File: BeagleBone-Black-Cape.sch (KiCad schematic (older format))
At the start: 2 parts

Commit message: FOUR LAYER BOARD CHANGE. We still need to adapt the other subsystems for four layers
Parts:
- gave numbers to parts that had none: 2
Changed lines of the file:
@@
 	3800 2900 3700 2900
 $Comp
-L BeagleBone-Black-Cape-rescue:Conn_02x23_Odd_Even-Connector_Generic P?
+L BeagleBone-Black-Cape-rescue:Conn_02x23_Odd_Even-Connector_Generic P101
 U 1 1 55DF7DBA
 P 4000 3600
-F 0 "P?" H 4000 4800 50  0000 C CNN
+F 0 "P101" H 4000 4800 50  0000 C CNN
 F 1 "BeagleBone_Black_Header" V 4050 3650 50  0000 C CNN
 F 2 "Socket_BeagleBone_Black:Socket_BeagleBone_Black" H 4000 2750 60  0001 C CNN
@@
 $EndComp
 $Comp
-L BeagleBone-Black-Cape-rescue:Conn_02x23_Odd_Even-Connector_Generic P?
+L BeagleBone-Black-Cape-rescue:Conn_02x23_Odd_Even-Connector_Generic P102
 U 1 1 55DF7DE1
 P 6200 3600
-F 0 "P?" H 6200 4800 50  0000 C CNN
+F 0 "P102" H 6200 4800 50  0000 C CNN
 F 1 "BeagleBone_Black_Header" V 6250 3650 50  0000 C CNN
 F 2 "Socket_BeagleBone_Black:Socket_BeagleBone_Black" H 6200 2750 60  0001 C CNN
@@
 $EndComp
 $Comp
-L power:GND #PWR0101
+L power:GND #PWR0107
 U 1 1 614B6213
 P 3000 2500
-F 0 "#PWR0101" H 3000 2250 50  0001 C CNN
+F 0 "#PWR0107" H 3000 2250 50  0001 C CNN
 F 1 "GND" H 3005 2327 50  0000 C CNN
 F 2 "" H 3000 2500 50  0001 C CNN

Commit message: Recovered the .lib for flash symbol. Relinked in schematic
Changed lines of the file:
@@
 	3650 4900 4050 4900
 $Comp
-L power:GND #PWR0105
+L BeagleBone-Black-Cape-rescue:GND-power #PWR0105
 U 1 1 614B4DBF
 P 4050 4900
@@
 	4050 4900 4450 4900
 $Comp
-L power:GND #PWR0109
+L BeagleBone-Black-Cape-rescue:GND-power #PWR0109
 U 1 1 614B5823
 P 5100 2500
@@
 $EndComp
 $Comp
-L power:GND #PWR0101
+L BeagleBone-Black-Cape-rescue:GND-power #PWR0101
 U 1 1 614B6213
 P 3000 2500
@@
 $EndComp
 $Comp
-L power:GND #PWR0110
+L BeagleBone-Black-Cape-rescue:GND-power #PWR0110
 U 1 1 614B8C07
 P 5750 2500
@@
 $EndComp
 $Comp
-L power:GND #PWR0111
+L BeagleBone-Black-Cape-rescue:GND-power #PWR0111
 U 1 1 614B962C
 P 6750 2500

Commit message: sync push so zach can work
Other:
- moved on the sheet: P101, P102

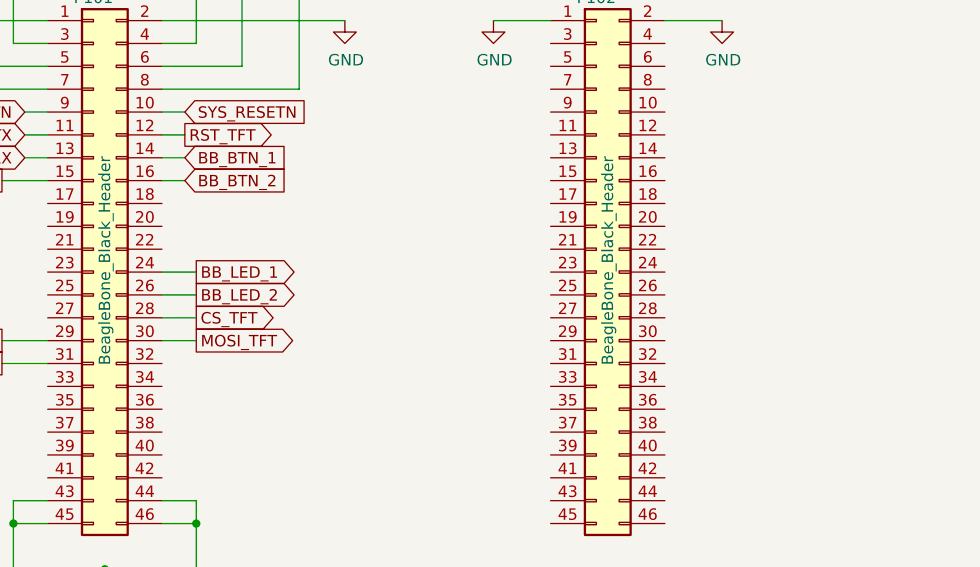
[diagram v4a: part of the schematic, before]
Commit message: Massive PCB/Schematic Update
The PCB has been completed, and the schematic has been updated to have the correct footprints
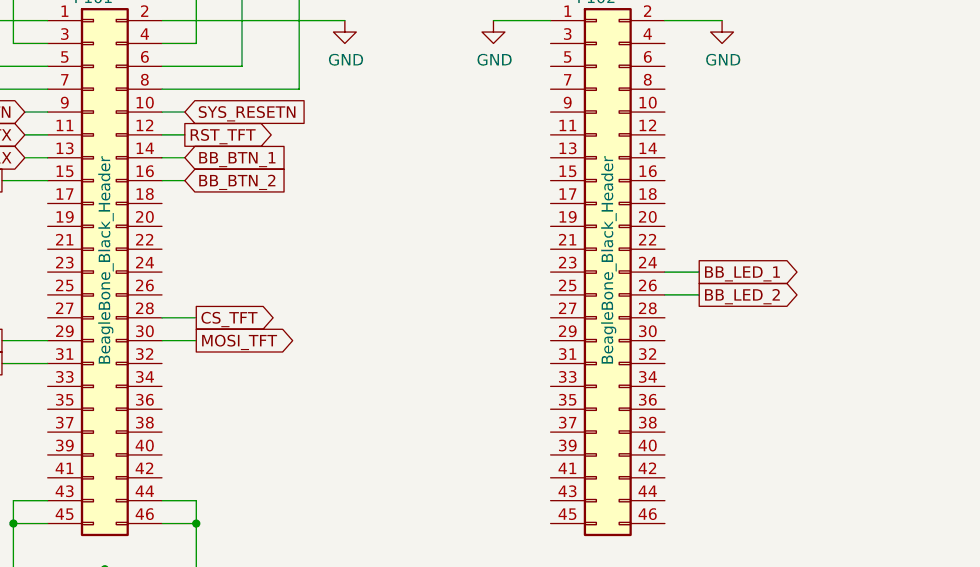
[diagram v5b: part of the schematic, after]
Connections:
- net BB_LED_1: now also P102.24 (Pin_24); no longer P101.24 (Pin_24)
- net BB_LED_2: now also P102.26 (Pin_26); no longer P101.26 (Pin_26)
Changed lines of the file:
@@
 F1 "MCU_subsystem.sch" 50
 $EndSheet
-Text GLabel 4450 3550 2    50   Output ~ 0
+Text GLabel 6650 3550 2    50   Output ~ 0
 BB_LED_1
-Text GLabel 4450 3650 2    50   Output ~ 0
+Text GLabel 6650 3650 2    50   Output ~ 0
 BB_LED_2
 Wire Wire Line
-	4300 3550 4450 3550
+	6500 3550 6650 3550
 Wire Wire Line
-	4300 3650 4450 3650
+	6500 3650 6650 3650
 $Comp
 L BeagleBone-Black-Cape-rescue:Conn_02x23_Odd_Even-Connector_Generic P102

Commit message: lib update so it only includes user-made library
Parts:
- P101, P102: symbol BeagleBone-Black-Cape-rescue:Conn_02x23_Odd_Even-Connector_Generic -> UserMade-BB-Zigbee-Gateway-CAPE:Conn_02x23_Odd_Even-Connector_Generic
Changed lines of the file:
@@
 Connection ~ 4450 4650
 $Comp
-L BeagleBone-Black-Cape-rescue:+3.3V-power #PWR0106
+L UserMade-BB-Zigbee-Gateway-CAPE:+3.3V-power #PWR0106
 U 1 1 55897A67
 P 4450 2250
@@
 $EndComp
 $Comp
-L BeagleBone-Black-Cape-rescue:+5V-power #PWR0107
+L UserMade-BB-Zigbee-Gateway-CAPE:+5V-power #PWR0107
 U 1 1 55897A7F
 P 4650 2250
@@
 	4900 2750 4300 2750
 $Comp
-L BeagleBone-Black-Cape-rescue:+3.3V-power #PWR0104
+L UserMade-BB-Zigbee-Gateway-CAPE:+3.3V-power #PWR0104
 U 1 1 55897EE7
 P 3650 2250
@@
 $EndComp
 $Comp
-L BeagleBone-Black-Cape-rescue:+5V-power #PWR0103
+L UserMade-BB-Zigbee-Gateway-CAPE:+5V-power #PWR0103
 U 1 1 55897EF8
 P 3450 2250
@@
 	6500 2450 6750 2450
 $Comp
-L pwr_BeagleBone:SYS_5V #PWR0108
+L UserMade-BB-Zigbee-Gateway-CAPE:SYS_5V #PWR0108
 U 1 1 55898497
 P 4900 2250
@@
 $EndComp
 $Comp
-L pwr_BeagleBone:SYS_5V #PWR0102
+L UserMade-BB-Zigbee-Gateway-CAPE:SYS_5V #PWR0102
 U 1 1 558984AF
 P 3200 2250
@@
 	3800 2850 3700 2850
 $Comp
-L BeagleBone-Black-Cape-rescue:Conn_02x23_Odd_Even-Connector_Generic P101
+L UserMade-BB-Zigbee-Gateway-CAPE:Conn_02x23_Odd_Even-Connector_Generic P101
 U 1 1 55DF7DBA
 P 4000 3550
@@
 	3650 4850 4050 4850
 $Comp
-L BeagleBone-Black-Cape-rescue:GND-power #PWR0105
+L UserMade-BB-Zigbee-Gateway-CAPE:GND-power #PWR0105
 U 1 1 614B4DBF
 P 4050 4850
@@
 	4050 4850 4450 4850
 $Comp
-L BeagleBone-Black-Cape-rescue:GND-power #PWR0109
+L UserMade-BB-Zigbee-Gateway-CAPE:GND-power #PWR0109
 U 1 1 614B5823
 P 5100 2450
@@
 $EndComp
 $Comp
-L BeagleBone-Black-Cape-rescue:GND-power #PWR0101
+L UserMade-BB-Zigbee-Gateway-CAPE:GND-power #PWR0101
 U 1 1 614B6213
 P 3000 2450
@@
 $EndComp
 $Comp
-L BeagleBone-Black-Cape-rescue:GND-power #PWR0110
+L UserMade-BB-Zigbee-Gateway-CAPE:GND-power #PWR0110
 U 1 1 614B8C07
 P 5750 2450
@@
 $EndComp
 $Comp
-L BeagleBone-Black-Cape-rescue:GND-power #PWR0111
+L UserMade-BB-Zigbee-Gateway-CAPE:GND-power #PWR0111
 U 1 1 614B962C
 P 6750 2450
@@
 	6500 3650 6650 3650
 $Comp
-L BeagleBone-Black-Cape-rescue:Conn_02x23_Odd_Even-Connector_Generic P102
+L UserMade-BB-Zigbee-Gateway-CAPE:Conn_02x23_Odd_Even-Connector_Generic P102
 U 1 1 55DF7DE1
 P 6200 3550
